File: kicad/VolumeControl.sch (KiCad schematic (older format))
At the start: 6 parts, among them P1 PWR_IN, P2 SOURCE_1, P3 SOURCE_2, P4 CONTROL, P5 AUDIO_OUT, P6 PWR_OUT

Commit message: Adding untracked files
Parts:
- removed P1: PWR_IN, Pin_Headers:Pin_Header_Straight_1x02, symbol CONN_01X02
- added P1: PWR_IN, JST:JST-3RA, symbol CONN_01X03
- added P7: AUDIO_OUT, JST:JST-4RA, symbol CONN_01X04
- P2: renamed from P6; footprint Pin_Headers:Pin_Header_Straight_1x02 -> JST:JST-2RA
- P3: renamed from P2; footprint Pin_Headers:Pin_Header_Straight_1x04 -> JST:JST-4RA
- P4: renamed from P3; footprint Pin_Headers:Pin_Header_Straight_1x04 -> JST:JST-4RA
- P5: renamed from P4; footprint Pin_Headers:Pin_Header_Straight_1x05 -> JST:JST-5RA
- P6: renamed from P5; footprint Pin_Headers:Pin_Header_Straight_1x04 -> JST:JST-4RA
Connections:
- net +12V: now also P1.2 (P2)
- net +5VD: now also P1.1 (P1)
- net Audio Processing/LEFT: now also P7.1 (P1)
- net Audio Processing/RIGHT: now also P7.4 (P4)
- net GNDA: now also P7.2 (P2), P7.3 (P3); no longer P3.2 (P2), P3.3 (P3), P4.2 (P2), P4.3 (P3)
- net GNDD: now also P3.2 (P2), P3.3 (P3), P4.2 (P2), P4.3 (P3), P1.3 (P3)
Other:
- moved on the sheet: P2, P3, P4

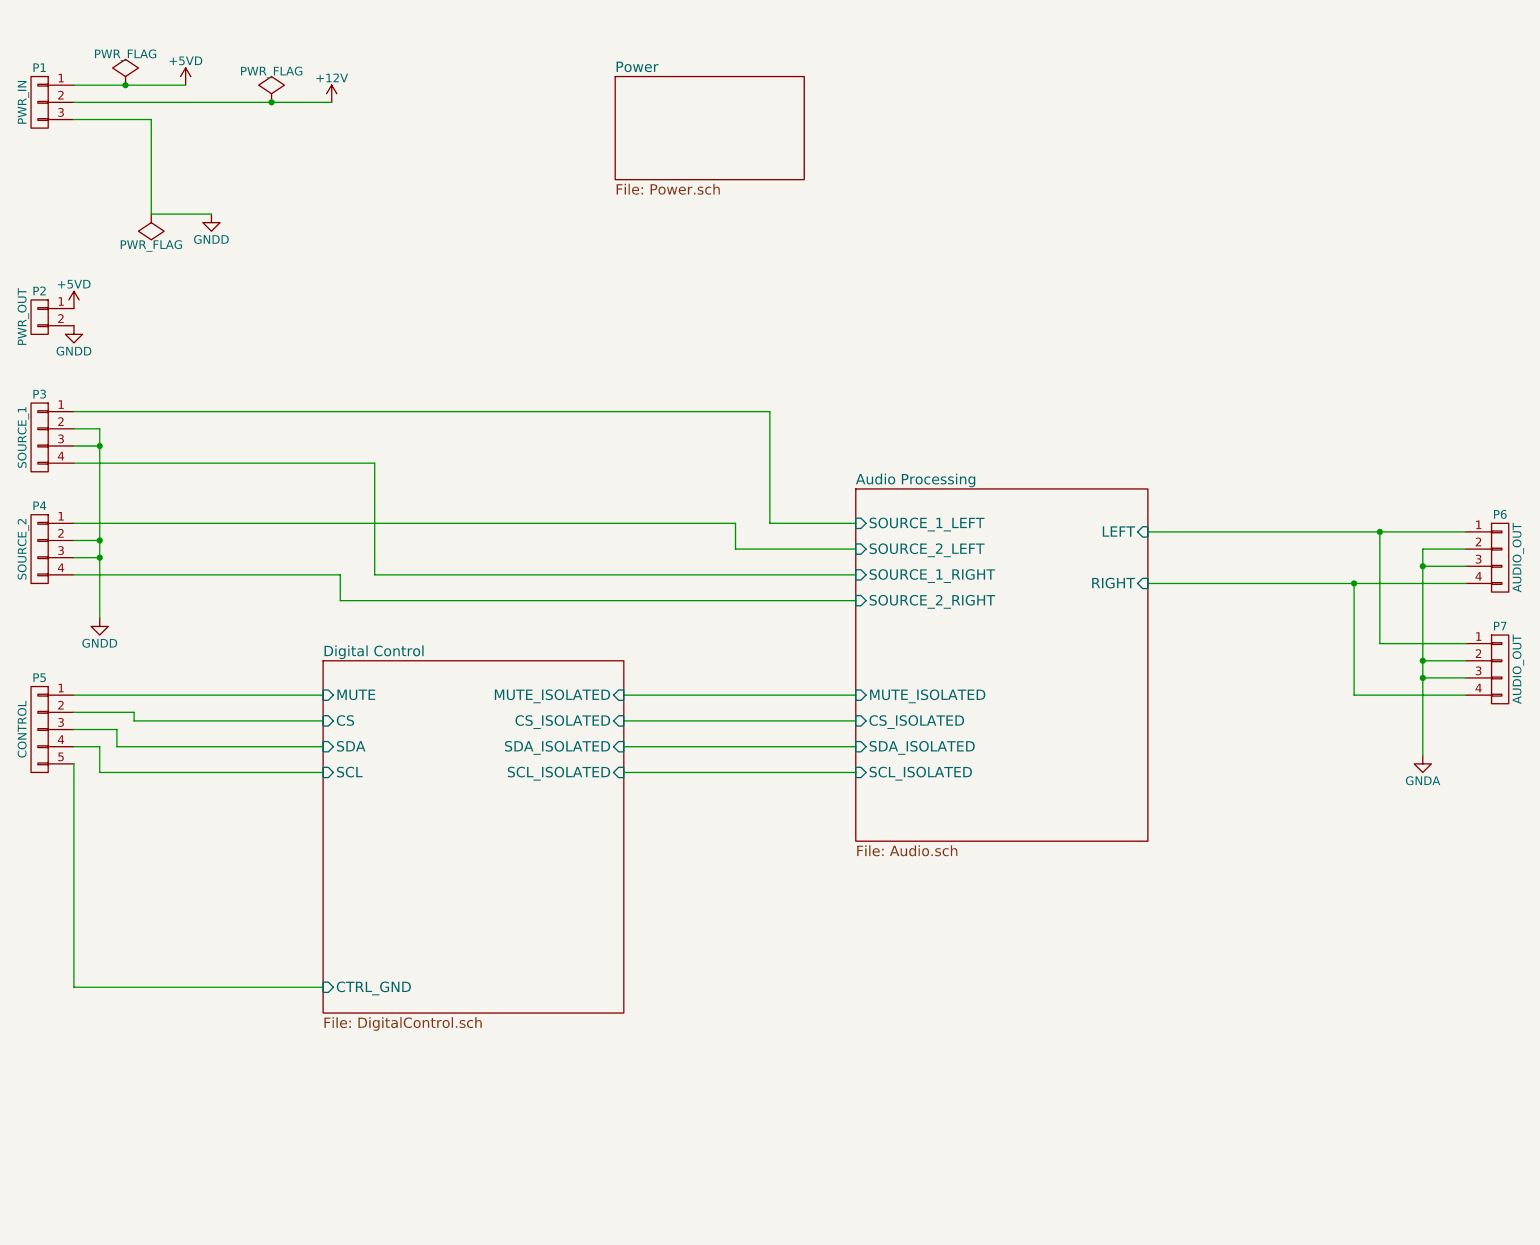
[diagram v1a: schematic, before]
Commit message: Reworked schematics to allow control of the power and introduction of ATMega328P for control
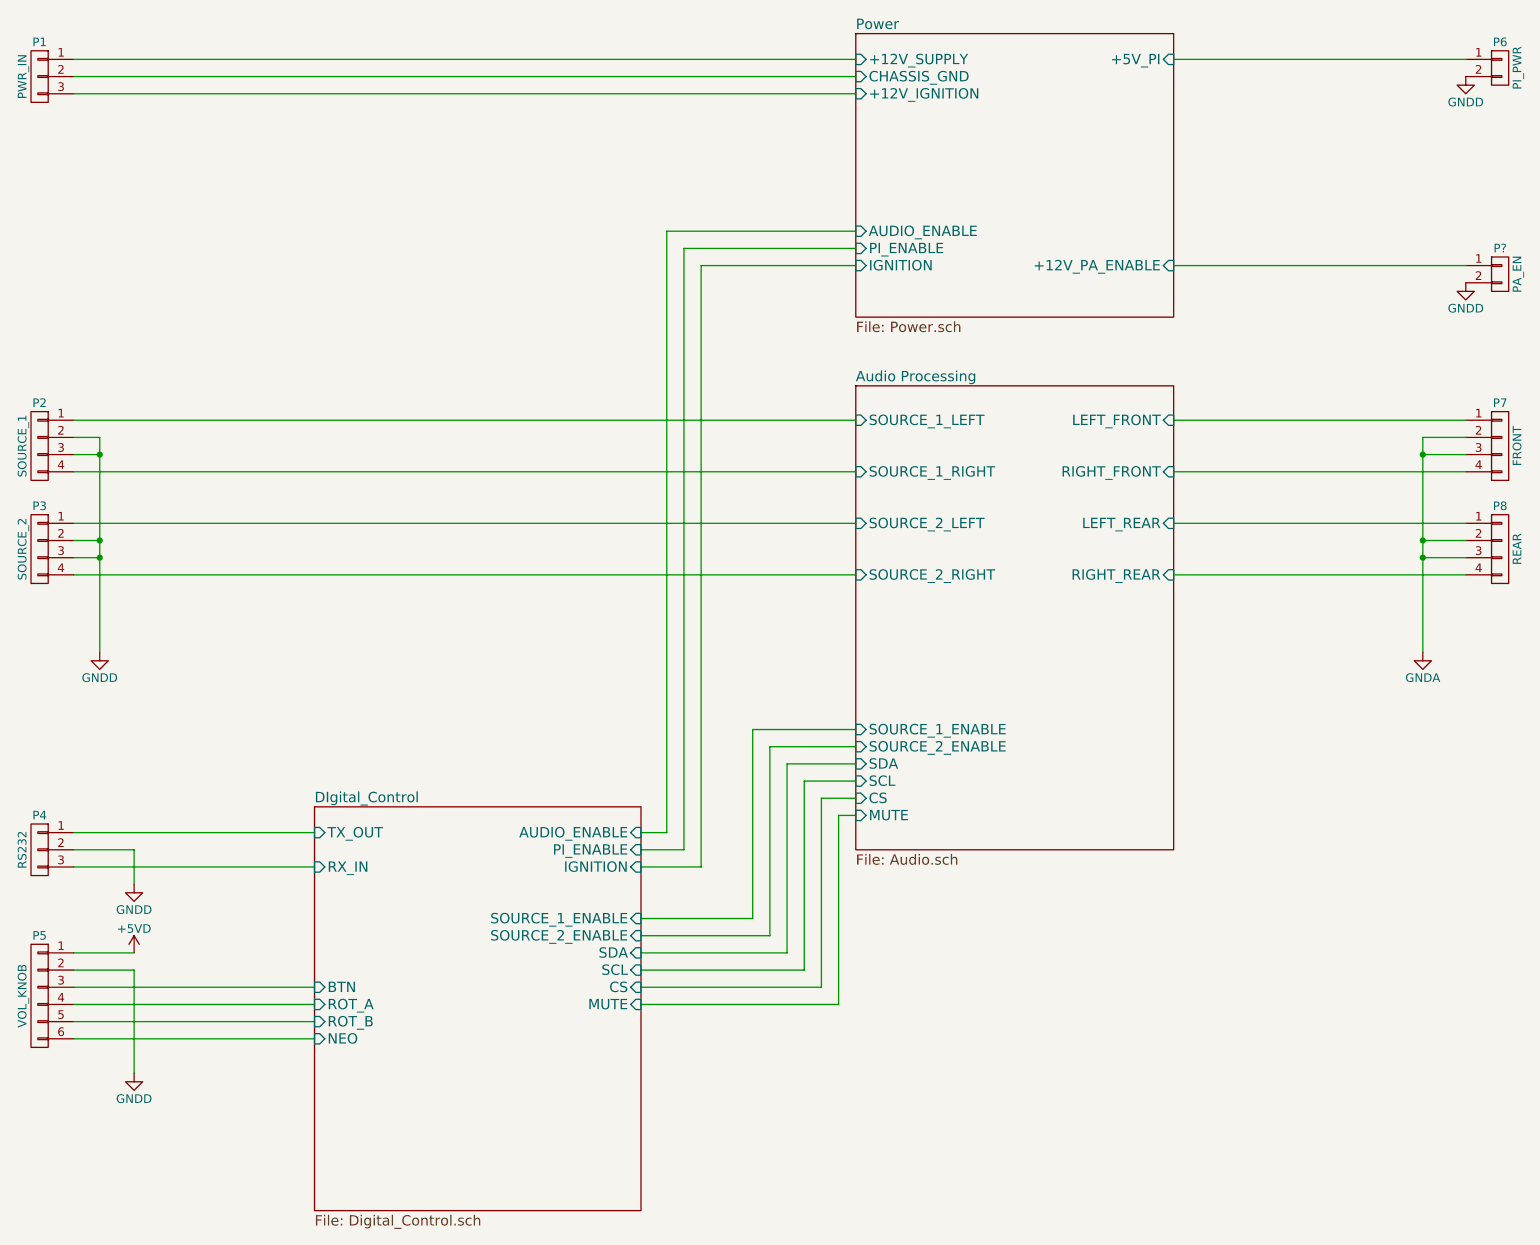
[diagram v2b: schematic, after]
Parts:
- removed P5: CONTROL, JST:JST-5RA, symbol CONN_01X05
- added P4: RS232, symbol CONN_01X03
- added P5: VOL_KNOB, symbol CONN_01X06
- added P?: PA_EN, symbol CONN_01X02
- P6: renamed from P2; value PWR_OUT -> PI_PWR
- P7: renamed from P6; value AUDIO_OUT -> FRONT
- P8: renamed from P7; value AUDIO_OUT -> REAR
- renumbered P3 to P2, P4 to P3
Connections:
- net +5VD: now also P5.1 (P1); no longer P1.1 (P1), P6.1 (P1)
- net GNDD: now also P4.2 (P2), P5.2 (P2), P?.2 (P2); no longer P1.3 (P3)
- net +12V renamed Power/CHASSIS_GND
- net Audio Processing/LEFT renamed Audio Processing/LEFT_FRONT
- net Audio Processing/LEFT_FRONT: no longer P8.1 (P1)
- net Audio Processing/RIGHT renamed Audio Processing/RIGHT_FRONT
- net Audio Processing/RIGHT_FRONT: no longer P8.4 (P4)
- new net Audio Processing/LEFT_REAR: P8.1 (P1)
- new net Audio Processing/RIGHT_REAR: P8.4 (P4)
- new net DIgital_Control/BTN: P5.3 (P3)
- new net DIgital_Control/NEO: P5.6 (P6)
- new net DIgital_Control/ROT_A: P5.4 (P4)
- new net DIgital_Control/ROT_B: P5.5 (P5)
- new net DIgital_Control/RX_IN: P4.3 (P3)
- new net DIgital_Control/TX_OUT: P4.1 (P1)
- new net Power/+12V_IGNITION: P1.3 (P3)
- new net Power/+12V_PA_ENABLE: P?.1 (P1)
- new net Power/+12V_SUPPLY: P1.1 (P1)
- new net Power/+5V_PI: P6.1 (P1)
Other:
- moved on the sheet: P1, P2, P6, P7, P8

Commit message: Produced Volume knob including Gerbers, and updated main board to remove ERC errors.  Just about to start board layout
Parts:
- P4: footprint (none) -> JST:JST-3RA
- P5: footprint (none) -> JST:JST-6RA
- P7: renamed from P?; footprint (none) -> JST:JST-2RA
- renumbered P7 to P8, P8 to P9
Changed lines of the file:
@@
 F8 "+5V_PI" I R 8350 900 60
 F9 "+12V_PA_ENABLE" I R 8350 2100 60
+F10 "PA_ENABLE" I L 6500 1800 60
 $EndSheet
 $Sheet
@@
 F12 "MUTE" I L 6500 5300 60
 F13 "CS" I L 6500 5200 60
-F14 "SCL" I L 6500 5100 60
-F15 "SDA" I L 6500 5000 60
+F14 "SDI" I L 6500 5000 60
+F15 "SCLK" I L 6500 5100 60
 $EndSheet
 $Comp
-L CONN_01X04 P7
+L CONN_01X04 P8
 U 1 1 56CB598D
 P 10250 3150
-F 0 "P7" H 10250 3400 50  0000 C CNN
+F 0 "P8" H 10250 3400 50  0000 C CNN
 F 1 "FRONT" V 10350 3150 50  0000 C CNN
 F 2 "JST:JST-4RA" H 10250 3150 50  0001 C CNN
@@
 $EndComp
 $Comp
-L GNDA #PWR5
+L GNDA #PWR01
 U 1 1 56CB66F2
 P 9800 4350
-F 0 "#PWR5" H 9800 4100 50  0001 C CNN
+F 0 "#PWR01" H 9800 4100 50  0001 C CNN
 F 1 "GNDA" H 9800 4200 50  0000 C CNN
 F 2 "" H 9800 4350 50  0000 C CNN
@@
 $EndComp
 $Comp
-L GNDD #PWR7
+L GNDD #PWR02
 U 1 1 56CB9AB4
 P 10050 1000
-F 0 "#PWR7" H 10050 750 50  0001 C CNN
+F 0 "#PWR02" H 10050 750 50  0001 C CNN
 F 1 "GNDD" H 10050 850 50  0000 C CNN
 F 2 "" H 10050 1000 50  0000 C CNN
@@
 $EndComp
 $Comp
-L GNDD #PWR1
+L GNDD #PWR03
 U 1 1 56F2B6D7
 P 2100 4350
-F 0 "#PWR1" H 2100 4100 50  0001 C CNN
+F 0 "#PWR03" H 2100 4100 50  0001 C CNN
 F 1 "GNDD" H 2100 4200 50  0000 C CNN
 F 2 "" H 2100 4350 50  0000 C CNN
@@
 $EndComp
 $Comp
-L CONN_01X04 P8
+L CONN_01X04 P9
 U 1 1 570D748D
 P 10250 3750
-F 0 "P8" H 10250 4000 50  0000 C CNN
+F 0 "P9" H 10250 4000 50  0000 C CNN
 F 1 "REAR" V 10350 3750 50  0000 C CNN
 F 2 "JST:JST-4RA" H 10250 3750 50  0001 C CNN
@@
 F 0 "P5" H 1750 6700 50  0000 C CNN
 F 1 "VOL_KNOB" V 1850 6350 50  0000 C CNN
-F 2 "" H 1750 6350 50  0000 C CNN
+F 2 "JST:JST-6RA" H 1750 6350 50  0001 C CNN
 F 3 "" H 1750 6350 50  0000 C CNN
 	1    1750 6350
@@
 F 0 "P4" H 1750 5700 50  0000 C CNN
 F 1 "RS232" V 1850 5500 50  0000 C CNN
-F 2 "" H 1750 5500 50  0000 C CNN
+F 2 "JST:JST-3RA" H 1750 5500 50  0001 C CNN
 F 3 "" H 1750 5500 50  0000 C CNN
 	1    1750 5500
 	-1   0    0    -1
 $EndComp
+Wire Wire Line
+	1950 6600 3350 6600
+Wire Wire Line
+	1950 6500 3350 6500
+Wire Wire Line
+	1950 6400 3350 6400
+Wire Wire Line
+	1950 6300 3350 6300
+Wire Wire Line
+	1950 6200 2300 6200
+Wire Wire Line
+	2300 6200 2300 6800
+$Comp
+L GNDD #PWR04
+U 1 1 575FF700
+P 2300 6800
+F 0 "#PWR04" H 2300 6550 50  0001 C CNN
+F 1 "GNDD" H 2300 6650 50  0000 C CNN
+F 2 "" H 2300 6800 50  0000 C CNN
+F 3 "" H 2300 6800 50  0000 C CNN
+	1    2300 6800
+	1    0    0    -1
+$EndComp
+$Comp
+L +5VD #PWR05
+U 1 1 575FF7C6
+P 2300 6100
+F 0 "#PWR05" H 2300 5950 50  0001 C CNN
+F 1 "+5VD" H 2300 6240 50  0000 C CNN
+F 2 "" H 2300 6100 50  0000 C CNN
+F 3 "" H 2300 6100 50  0000 C CNN
+	1    2300 6100
+	1    0    0    -1
+$EndComp
+Wire Wire Line
+	1950 6100 2300 6100
+Wire Wire Line
+	1950 5400 3350 5400
+Wire Wire Line
+	1950 5600 3350 5600
+Wire Wire Line
+	1950 5500 2300 5500
+Wire Wire Line
+	2300 5500 2300 5700
+$Comp
+L GNDD #PWR06
+U 1 1 575FFC73
+P 2300 5700
+F 0 "#PWR06" H 2300 5450 50  0001 C CNN
+F 1 "GNDD" H 2300 5550 50  0000 C CNN
+F 2 "" H 2300 5700 50  0000 C CNN
+F 3 "" H 2300 5700 50  0000 C CNN
+	1    2300 5700
+	1    0    0    -1
+$EndComp
+Wire Wire Line
+	5250 6400 6400 6400
+Wire Wire Line
+	6400 6400 6400 5300
+Wire Wire Line
+	6400 5300 6500 5300
+Wire Wire Line
+	5250 6300 6300 6300
+Wire Wire Line
+	6300 6300 6300 5200
+Wire Wire Line
+	6300 5200 6500 5200
+Wire Wire Line
+	5250 6000 6000 6000
+Wire Wire Line
+	6000 6000 6000 4900
+Wire Wire Line
+	6000 4900 6500 4900
+Wire Wire Line
+	5250 5900 5900 5900
+Wire Wire Line
+	5900 5900 5900 4800
+Wire Wire Line
+	5900 4800 6500 4800
+Wire Wire Line
+	1950 3000 6500 3000
+Wire Wire Line
+	1950 3300 6500 3300
+Wire Wire Line
+	1950 3600 6500 3600
+Wire Wire Line
+	1950 3900 6500 3900
+Wire Wire Line
+	10050 3100 9800 3100
+Wire Wire Line
+	9800 3100 9800 4350
+Wire Wire Line
+	8350 3000 10050 3000
+Wire Wire Line
+	10050 3300 8350 3300
+Wire Wire Line
+	8350 3600 10050 3600
+Wire Wire Line
+	10050 3900 8350 3900
+Wire Wire Line
+	5250 5600 5600 5600
+Wire Wire Line
+	5600 5600 5600 2100
+Wire Wire Line
+	5600 2100 6500 2100
+Wire Wire Line
+	5250 5500 5500 5500
+Wire Wire Line
+	5500 5500 5500 2000
+Wire Wire Line
+	5500 2000 6500 2000
+Wire Wire Line
+	5250 5400 5400 5400
+Wire Wire Line
+	5400 5400 5400 1900
+Wire Wire Line
+	5400 1900 6500 1900
+Wire Wire Line
+	8350 900  10050 900
+Wire Wire Line
+	1950 900  6500 900
+Wire Wire Line
+	1950 1000 6500 1000
+Wire Wire Line
+	1950 1100 6500 1100
+$Comp
+L CONN_01X02 P7
+U 1 1 57608D54
+P 10250 2150
+F 0 "P7" H 10250 2300 50  0000 C CNN
+F 1 "PA_EN" V 10350 2150 50  0000 C CNN
+F 2 "JST:JST-2RA" H 10250 2150 50  0001 C CNN
+F 3 "" H 10250 2150 50  0000 C CNN
+	1    10250 2150
+	1    0    0    -1
+$EndComp
+Wire Wire Line
+	8350 2100 10050 2100
+$Comp
+L GNDD #PWR07
+U 1 1 57608FA6
+P 10050 2200
+F 0 "#PWR07" H 10050 1950 50  0001 C CNN
+F 1 "GNDD" H 10050 2050 50  0000 C CNN
+F 2 "" H 10050 2200 50  0000 C CNN
+F 3 "" H 10050 2200 50  0000 C CNN
+	1    10050 2200
+	1    0    0    -1
+$EndComp
+Wire Wire Line
+	5250 5300 5300 5300
+Wire Wire Line
+	5300 5300 5300 1800
+Wire Wire Line
+	5300 1800 6500 1800
 $Sheet
 S 3350 5250 1900 2350
@@
 F11 "MUTE" I R 5250 6400 60
 F12 "CS" I R 5250 6300 60
-F13 "SDA" I R 5250 6100 60
-F14 "SCL" I R 5250 6200 60
-F15 "SOURCE_1_ENABLE" I R 5250 5900 60
-F16 "SOURCE_2_ENABLE" I R 5250 6000 60
+F13 "SOURCE_1_ENABLE" I R 5250 5900 60
+F14 "SOURCE_2_ENABLE" I R 5250 6000 60
+F15 "PA_ENABLE" I R 5250 5300 60
+F16 "SDI" I R 5250 6100 60
+F17 "SCLK" I R 5250 6200 60
 $EndSheet
 Wire Wire Line
-	1950 6600 3350 6600
-Wire Wire Line
-	1950 6500 3350 6500
-Wire Wire Line
-	1950 6400 3350 6400
-Wire Wire Line
-	1950 6300 3350 6300
-Wire Wire Line
-	1950 6200 2300 6200
-Wire Wire Line
-	2300 6200 2300 6800
-$Comp
-L GNDD #PWR4
-U 1 1 575FF700
-P 2300 6800
-F 0 "#PWR4" H 2300 6550 50  0001 C CNN
-F 1 "GNDD" H 2300 6650 50  0000 C CNN
-F 2 "" H 2300 6800 50  0000 C CNN
-F 3 "" H 2300 6800 50  0000 C CNN
-	1    2300 6800
-	1    0    0    -1
-$EndComp
-$Comp
-L +5VD #PWR3
-U 1 1 575FF7C6
-P 2300 6100
-F 0 "#PWR3" H 2300 5950 50  0001 C CNN
-F 1 "+5VD" H 2300 6240 50  0000 C CNN
-F 2 "" H 2300 6100 50  0000 C CNN
-F 3 "" H 2300 6100 50  0000 C CNN
-	1    2300 6100
-	1    0    0    -1
-$EndComp
-Wire Wire Line
-	1950 6100 2300 6100
-Wire Wire Line
-	1950 5400 3350 5400
-Wire Wire Line
-	1950 5600 3350 5600
-Wire Wire Line
-	1950 5500 2300 5500
-Wire Wire Line
-	2300 5500 2300 5700
-$Comp
-L GNDD #PWR2
-U 1 1 575FFC73
-P 2300 5700
-F 0 "#PWR2" H 2300 5450 50  0001 C CNN
-F 1 "GNDD" H 2300 5550 50  0000 C CNN
-F 2 "" H 2300 5700 50  0000 C CNN
-F 3 "" H 2300 5700 50  0000 C CNN
-	1    2300 5700
-	1    0    0    -1
-$EndComp
-Wire Wire Line
-	5250 6400 6400 6400
-Wire Wire Line
-	6400 6400 6400 5300
-Wire Wire Line
-	6400 5300 6500 5300
-Wire Wire Line
-	5250 6300 6300 6300
-Wire Wire Line
-	6300 6300 6300 5200
-Wire Wire Line
-	6300 5200 6500 5200
+	5250 6100 6100 6100
+Wire Wire Line
+	6100 6100 6100 5000
+Wire Wire Line
+	6100 5000 6500 5000
 Wire Wire Line
 	5250 6200 6200 6200
@@
 Wire Wire Line
 	6200 5100 6500 5100
-Wire Wire Line
-	5250 6100 6100 6100
-Wire Wire Line
-	6100 6100 6100 5000
-Wire Wire Line
-	6100 5000 6500 5000
-Wire Wire Line
-	5250 6000 6000 6000
-Wire Wire Line
-	6000 6000 6000 4900
-Wire Wire Line
-	6000 4900 6500 4900
-Wire Wire Line
-	5250 5900 5900 5900
-Wire Wire Line
-	5900 5900 5900 4800
-Wire Wire Line
-	5900 4800 6500 4800
-Wire Wire Line
-	1950 3000 6500 3000
-Wire Wire Line
-	1950 3300 6500 3300
-Wire Wire Line
-	1950 3600 6500 3600
-Wire Wire Line
-	1950 3900 6500 3900
-Wire Wire Line
-	10050 3100 9800 3100
-Wire Wire Line
-	9800 3100 9800 4350
-Wire Wire Line
-	8350 3000 10050 3000
-Wire Wire Line
-	10050 3300 8350 3300
-Wire Wire Line
-	8350 3600 10050 3600
-Wire Wire Line
-	10050 3900 8350 3900
-Wire Wire Line
-	5250 5600 5600 5600
-Wire Wire Line
-	5600 5600 5600 2100
-Wire Wire Line
-	5600 2100 6500 2100
-Wire Wire Line
-	5250 5500 5500 5500
-Wire Wire Line
-	5500 5500 5500 2000
-Wire Wire Line
-	5500 2000 6500 2000
-Wire Wire Line
-	5250 5400 5400 5400
-Wire Wire Line
-	5400 5400 5400 1900
-Wire Wire Line
-	5400 1900 6500 1900
-Wire Wire Line
-	8350 900  10050 900
-Wire Wire Line
-	1950 900  6500 900
-Wire Wire Line
-	1950 1000 6500 1000
-Wire Wire Line
-	1950 1100 6500 1100
-$Comp
-L CONN_01X02 P?
-U 1 1 57608D54
-P 10250 2150
-F 0 "P?" H 10250 2300 50  0000 C CNN
-F 1 "PA_EN" V 10350 2150 50  0000 C CNN
-F 2 "" H 10250 2150 50  0000 C CNN
-F 3 "" H 10250 2150 50  0000 C CNN
-	1    10250 2150
-	1    0    0    -1
-$EndComp
-Wire Wire Line
-	8350 2100 10050 2100
-$Comp
-L GNDD #PWR?
-U 1 1 57608FA6
-P 10050 2200
-F 0 "#PWR?" H 10050 1950 50  0001 C CNN
-F 1 "GNDD" H 10050 2050 50  0000 C CNN
-F 2 "" H 10050 2200 50  0000 C CNN
-F 3 "" H 10050 2200 50  0000 C CNN
-	1    10050 2200
-	1    0    0    -1
-$EndComp
 $EndSCHEMATC
